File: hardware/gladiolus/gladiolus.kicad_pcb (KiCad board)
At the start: 4 copper layers, 70.7 x 53.3 mm, 7 parts, among them J1 NEIGHBOR1, J2 NEIGHBOR2, J7 BONUS_ROW

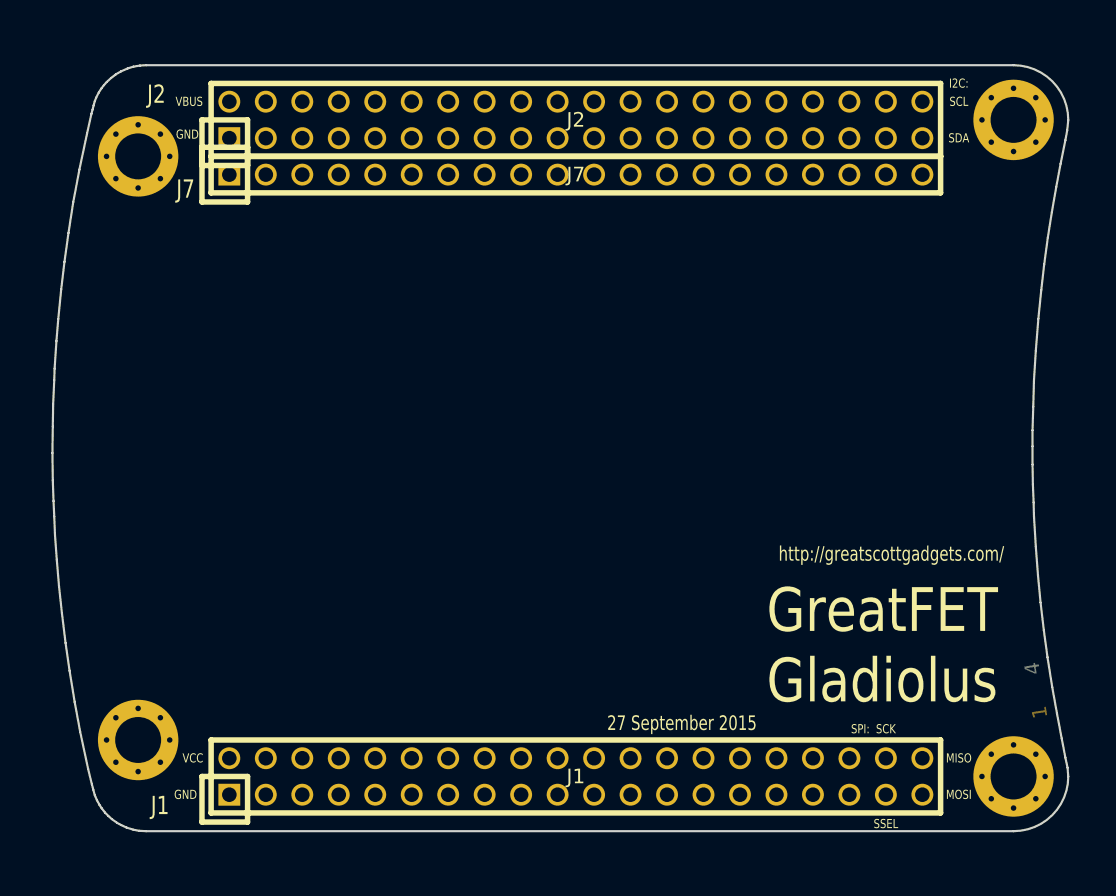
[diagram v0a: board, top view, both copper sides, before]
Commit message: Gladiolus: initial parts placement
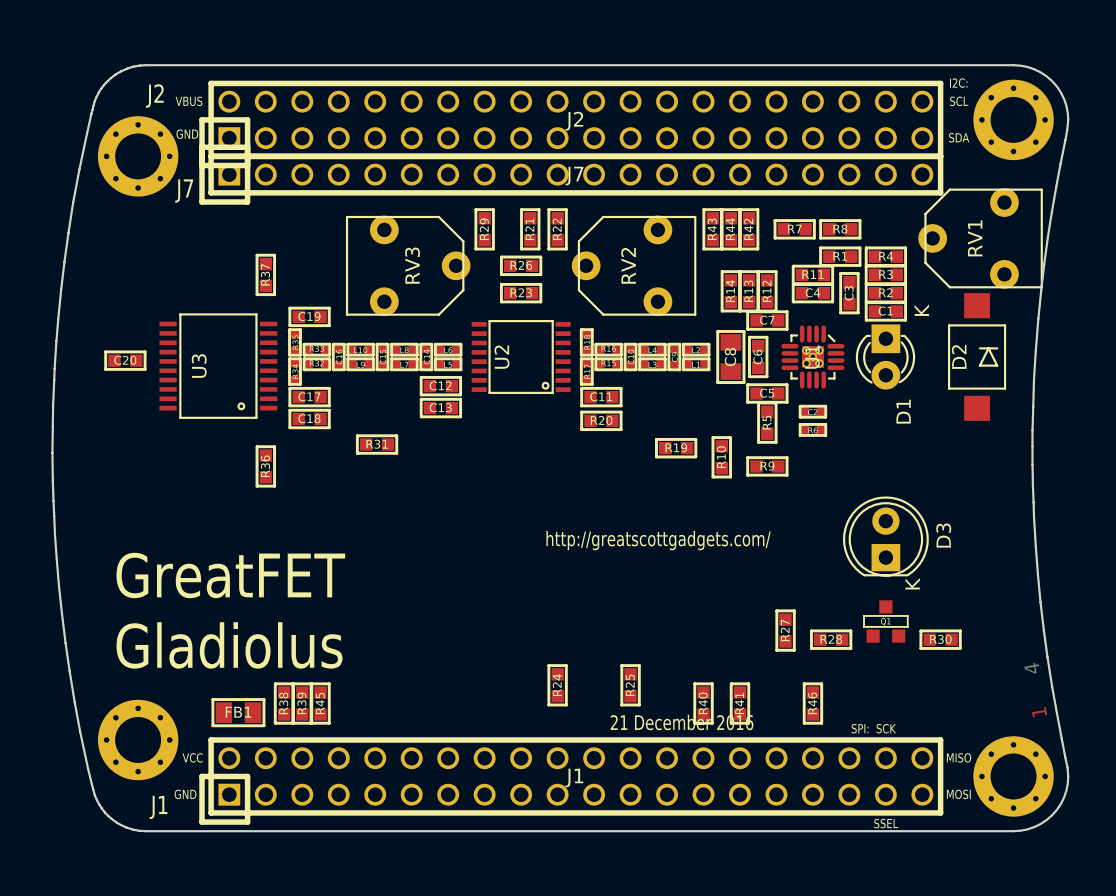
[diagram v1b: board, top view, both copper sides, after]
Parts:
- added C1: C, gsg-modules:0603, F.Cu at (167.6, 85.7)
- added C10: 15pF, gsg-modules:0402, F.Cu at (149.9, 88.9)
- added C11: 100nF, gsg-modules:0603, F.Cu at (147.8, 91.7)
- added C12: 100nF, gsg-modules:0603, F.Cu at (136.7, 90.9)
- added C13: 100nF, gsg-modules:0603, F.Cu at (136.7, 92.5)
- added C14: 130pF, gsg-modules:0402, F.Cu at (135.6, 88.9)
- added C15: 82pF, gsg-modules:0402, F.Cu at (132.6, 88.9)
- added C16: 24pF, gsg-modules:0402, F.Cu at (129.5, 88.9)
- added C17: 100nF, gsg-modules:0603, F.Cu at (127.5, 91.7)
- added C18: 100nF, gsg-modules:0603, F.Cu at (127.5, 93.2)
- added C19: 100nF, gsg-modules:0603, F.Cu at (127.5, 86.1)
- added C2: 15pF, gsg-modules:0402, F.Cu at (162.6, 92.7)
- added C20: 100nF, gsg-modules:0603, F.Cu at (114.7, 89.2)
- added C3: 100nF, gsg-modules:0603, F.Cu at (165.1, 84.5)
- added C4: C, gsg-modules:0603, F.Cu at (162.6, 84.5)
- added C5: 100nF, gsg-modules:0603, F.Cu at (159.4, 91.4)
- added C6: 100nF, gsg-modules:0603, F.Cu at (158.8, 88.9)
- added C7: 100nF, gsg-modules:0603, F.Cu at (159.4, 86.4)
- added C8: 10uF, gsg-modules:0805, F.Cu at (156.8, 88.9)
- added C9: 100pF, gsg-modules:0402, F.Cu at (152.9, 88.9)
- added D1: PHOTODIODE, LEDs:LED-3MM, F.Cu at (167.6, 87.6)
- added D2: PHOTODIODE, gsg-modules:VBPW34FASR, F.Cu at (174.0, 88.9)
- added D3: LED, LEDs:LED-5MM, F.Cu at (167.6, 102.9)
- added FB1: FILTER, gsg-modules:0805, F.Cu at (122.6, 113.7)
- added L1: 2.2uH, gsg-modules:0402, F.Cu at (154.4, 89.4)
- added L10: 1uH, gsg-modules:0402, F.Cu at (131.1, 88.4)
- added L2: 2.2uH, gsg-modules:0402, F.Cu at (154.4, 88.4)
- added L3: 1.5uH, gsg-modules:0402, F.Cu at (151.4, 89.4)
- added L4: 1.5uH, gsg-modules:0402, F.Cu at (151.4, 88.4)
- added L5: 2.2uH, gsg-modules:0402, F.Cu at (137.2, 89.4)
- added L6: 2.2uH, gsg-modules:0402, F.Cu at (137.2, 88.4)
- added L7: 2.2uH, gsg-modules:0402, F.Cu at (134.1, 89.4)
- added L8: 2.2uH, gsg-modules:0402, F.Cu at (134.1, 88.4)
- added L9: 1uH, gsg-modules:0402, F.Cu at (131.1, 89.4)
- added Q1: Q_NPN_BEC, gsg-modules:SOT23-3, F.Cu at (167.6, 107.3)
- added R1: 0, gsg-modules:0603, F.Cu at (164.5, 81.9)
- added R10: 10k, gsg-modules:0603, F.Cu at (156.2, 95.9)
- added R11: R, gsg-modules:0603, F.Cu at (162.6, 83.2)
- added R12: R, gsg-modules:0603, F.Cu at (159.4, 84.3)
- added R13: R, gsg-modules:0603, F.Cu at (158.1, 84.3)
- added R14: R, gsg-modules:0603, F.Cu at (156.8, 84.3)
- added R15: 0, gsg-modules:0402, F.Cu at (148.3, 89.4)
- added R16: 0, gsg-modules:0402, F.Cu at (148.3, 88.4)
- added R17: R, gsg-modules:0402, F.Cu at (146.8, 89.9)
- added R18: R, gsg-modules:0402, F.Cu at (146.8, 87.9)
- added R19: 0, gsg-modules:0603, F.Cu at (153.0, 95.2)
- added R2: 0, gsg-modules:0603, F.Cu at (167.6, 84.5)
- added R20: 0, gsg-modules:0603, F.Cu at (147.8, 93.3)
- added R21: 0, gsg-modules:0603, F.Cu at (142.9, 80.0)
- added R22: 0, gsg-modules:0603, F.Cu at (144.8, 80.0)
- added R23: 0, gsg-modules:0603, F.Cu at (142.2, 84.5)
- added R24: 0, gsg-modules:0603, F.Cu at (144.8, 111.8)
- added R25: 0, gsg-modules:0603, F.Cu at (149.9, 111.8)
- added R26: 0, gsg-modules:0603, F.Cu at (142.2, 82.5)
- added R27: 10k, gsg-modules:0603, F.Cu at (160.7, 108.0)
- added R28: 1k, gsg-modules:0603, F.Cu at (163.8, 108.6)
- added R29: 0, gsg-modules:0603, F.Cu at (139.7, 80.0)
- added R3: 0, gsg-modules:0603, F.Cu at (167.6, 83.2)
- added R30: 75, gsg-modules:0603, F.Cu at (171.4, 108.6)
- added R31: 0, gsg-modules:0603, F.Cu at (132.2, 95.0)
- added R32: 0, gsg-modules:0402, F.Cu at (128.0, 89.4)
- added R33: 0, gsg-modules:0402, F.Cu at (128.0, 88.4)
- added R34: R, gsg-modules:0402, F.Cu at (126.5, 89.9)
- added R35: R, gsg-modules:0402, F.Cu at (126.5, 87.9)
- added R36: 10k, gsg-modules:0603, F.Cu at (124.5, 96.5)
- added R37: R, gsg-modules:0603, F.Cu at (124.5, 83.2)
- added R38: 39, gsg-modules:0603, F.Cu at (125.7, 113.0)
- added R39: 39, gsg-modules:0603, F.Cu at (127.0, 113.0)
- added R4: 0, gsg-modules:0603, F.Cu at (167.6, 81.9)
- added R40: 39, gsg-modules:0603, F.Cu at (154.9, 113.0)
- added R41: 39, gsg-modules:0603, F.Cu at (157.5, 113.0)
- added R42: 39, gsg-modules:0603, F.Cu at (158.1, 80.0)
- added R43: 39, gsg-modules:0603, F.Cu at (155.6, 80.0)
- added R44: 39, gsg-modules:0603, F.Cu at (156.8, 80.0)
- added R45: 39, gsg-modules:0603, F.Cu at (128.3, 113.0)
- added R46: 39, gsg-modules:0603, F.Cu at (162.6, 113.0)
- added R5: R, gsg-modules:0603, F.Cu at (159.4, 93.5)
- added R6: 100k, gsg-modules:0402, F.Cu at (162.6, 94.0)
- added R7: 3.24k, gsg-modules:0603, F.Cu at (161.3, 80.0)
- added R8: 1.74k, gsg-modules:0603, F.Cu at (164.5, 80.0)
- added R9: 0, gsg-modules:0603, F.Cu at (159.4, 96.5)
- added RV1: POT, gsg-modules:3306F, F.Cu at (175.9, 80.6)
- added RV2: POT, gsg-modules:3306F, F.Cu at (151.8, 82.5)
- added RV3: POT, gsg-modules:3306F, F.Cu at (132.7, 82.5)
- added U1: THS4520RGT, gsg-modules:QFN16-3, F.Cu at (162.6, 88.9)
- added U2: AD8330ARQZ, gsg-modules:TSSOP16, F.Cu at (142.2, 88.9)
- added U3: AD9283, gsg-modules:SSOP20, F.Cu at (121.2, 89.5)
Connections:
- J1 pad 10: (no net) -> /P1_1
- J1 pad 11: (no net) -> /CLK0
- J1 pad 12: (no net) -> /P1_2
- J1 pad 13: (no net) -> /P1_5
- J1 pad 14: (no net) -> /P5_2
- J1 pad 15: (no net) -> /P1_7
- J1 pad 16: (no net) -> /P1_6
- J1 pad 17: (no net) -> /P1_9
- J1 pad 18: (no net) -> /P1_8
- J1 pad 19: (no net) -> /P5_3
- J1 pad 2: VCC -> Net-(FB1-Pad2)
- J1 pad 20: (no net) -> /P1_10
- J1 pad 21: (no net) -> /P1_12
- J1 pad 22: (no net) -> /P1_11
- J1 pad 23: (no net) -> /P5_5
- J1 pad 24: (no net) -> /P5_4
- J1 pad 25: (no net) -> /P1_14
- J1 pad 26: (no net) -> /P1_13
- J1 pad 27: (no net) -> /P5_6
- J1 pad 28: (no net) -> /P1_15
- J1 pad 29: (no net) -> /P5_7
- J1 pad 3: (no net) -> /P4_9
- J1 pad 30: (no net) -> /P1_16
- J1 pad 31: (no net) -> /P1_18
- J1 pad 32: (no net) -> /P1_17
- J1 pad 33: (no net) -> /P9_5
- J1 pad 34: (no net) -> /P9_6
- J1 pad 35: (no net) -> /P2_0
- J1 pad 36: (no net) -> /P6_0
- J1 pad 37: (no net) -> /P1_20
- J1 pad 38: (no net) -> /P1_19
- J1 pad 39: (no net) -> /P1_4
- J1 pad 4: (no net) -> /P0_0
- J1 pad 40: (no net) -> /P1_3
- J1 pad 5: (no net) -> /P4_10
- J1 pad 6: (no net) -> /P0_1
- J1 pad 7: (no net) -> /P1_0
- J1 pad 8: (no net) -> /P5_0
- J1 pad 9: (no net) -> /P5_1
- J2 pad 10: (no net) -> /P4_6
- J2 pad 11: (no net) -> /P4_7
- J2 pad 12: (no net) -> /CLK2
- J2 pad 13: (no net) -> /P2_8
- J2 pad 14: (no net) -> /P2_7
- J2 pad 15: (no net) -> /P2_6
- J2 pad 16: (no net) -> /P7_7
- J2 pad 17: (no net) -> /WAKEUP0
- J2 pad 18: (no net) -> /P2_5
- J2 pad 19: (no net) -> /P2_4
- J2 pad 20: (no net) -> /P2_3
- J2 pad 21: (no net) -> /PF_4
- J2 pad 22: (no net) -> /P3_2
- J2 pad 23: (no net) -> /P7_2
- J2 pad 24: (no net) -> /P3_1
- J2 pad 25: (no net) -> /P7_1
- J2 pad 26: (no net) -> /P3_0
- J2 pad 27: (no net) -> /P7_0
- J2 pad 28: (no net) -> /P3_4
- J2 pad 29: (no net) -> /P6_8
- J2 pad 3: (no net) -> /P4_8
- J2 pad 30: (no net) -> /P3_7
- J2 pad 31: (no net) -> /P6_7
- J2 pad 32: (no net) -> /P3_3
- J2 pad 33: (no net) -> /P2_2
- J2 pad 34: (no net) -> /P6_6
- J2 pad 35: (no net) -> /P2_1
- J2 pad 36: (no net) -> /P6_3
- J2 pad 37: (no net) -> /P3_5
- J2 pad 38: (no net) -> /P3_6
- J2 pad 39: (no net) -> /I2C0_SDA
- J2 pad 4: (no net) -> /P4_0
- J2 pad 40: (no net) -> /I2C0_SCL
- J2 pad 5: (no net) -> /ADC0_0
- J2 pad 6: (no net) -> /P4_5
- J2 pad 7: (no net) -> /P4_4
- J2 pad 8: (no net) -> /P4_2
- J2 pad 9: (no net) -> /P4_3
- J7 pad 11: (no net) -> /RESET
- J7 pad 12: (no net) -> /VBAT
- J7 pad 13: (no net) -> /P2_11
- J7 pad 14: (no net) -> /P2_10
- J7 pad 15: (no net) -> /P6_10
- J7 pad 16: (no net) -> /P6_9
- J7 pad 17: (no net) -> /P6_2
- J7 pad 18: (no net) -> /P6_1
- J7 pad 2: (no net) -> /P6_4
- J7 pad 20: VCC -> Net-(J7-Pad20)
- J7 pad 3: (no net) -> /P6_5
- J7 pad 4: (no net) -> /ADC0_5
- J7 pad 5: (no net) -> /ADC0_2
- J7 pad 6: (no net) -> /P2_9
- J7 pad 7: (no net) -> /P2_12
- J7 pad 8: (no net) -> /P2_13
- J7 pad 9: (no net) -> /RTC_ALARM
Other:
- board text added: "21 December 2016"
- board text removed: "27 September 2015"

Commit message: Gladiolus: reversed potentiometers
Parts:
- turned R43 to 270 degrees
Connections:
- RV1 pad 1: VCC -> GND
- RV1 pad 3: GND -> VCC
- RV2 pad 1: VCC -> GND
- RV2 pad 3: GND -> VCC
- RV3 pad 1: VCC -> GND
- RV3 pad 3: GND -> VCC
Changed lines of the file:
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@@
     (links 228)
     (no_connects 172)
-    (area 63.017399 66.04 279.525801 196.007778)
+    (area 109.525999 68.504999 180.415001 121.995001)
     (thickness 1.6)
     (drawings 122)
@@
   )
   (module gsg-modules:0603 (layer F.Cu)
-    (at 155.575 80.01 90)
-    (solder_mask_margin 0.1016)
-    (fp_text reference R43 (at 0 0 90) (layer F.SilkS)
-      (effects (font (size 0.6096 0.6096) (thickness 0.1524)))
-    )
-    (fp_text value 39 (at 0 0 90) (layer F.SilkS) hide
-      (effects (font (size 0.6096 0.6096) (thickness 0.1524)))
-    )
-    (fp_line (start 1.3716 -0.6096) (end -1.3716 -0.6096) (layer F.SilkS) (width 0.2032))
-    (fp_line (start -1.3716 -0.6096) (end -1.3716 0.6096) (layer F.SilkS) (width 0.2032))
-    (fp_line (start -1.3716 0.6096) (end 1.3716 0.6096) (layer F.SilkS) (width 0.2032))
-    (fp_line (start 1.3716 0.6096) (end 1.3716 -0.6096) (layer F.SilkS) (width 0.2032))
-    (pad 2 smd rect (at 0.762 0 90) (size 0.8636 0.8636) (layers F.Cu F.Paste F.Mask)
+    (at 155.575 80.01 270)
+    (solder_mask_margin 0.1016)
+    (fp_text reference R43 (at 0 0 270) (layer F.SilkS)
+      (effects (font (size 0.6096 0.6096) (thickness 0.1524)))
+    )
+    (fp_text value 39 (at 0 0 270) (layer F.SilkS) hide
+      (effects (font (size 0.6096 0.6096) (thickness 0.1524)))
+    )
+    (fp_line (start 1.3716 -0.6096) (end -1.3716 -0.6096) (layer F.SilkS) (width 0.2032))
+    (fp_line (start -1.3716 -0.6096) (end -1.3716 0.6096) (layer F.SilkS) (width 0.2032))
+    (fp_line (start -1.3716 0.6096) (end 1.3716 0.6096) (layer F.SilkS) (width 0.2032))
+    (fp_line (start 1.3716 0.6096) (end 1.3716 -0.6096) (layer F.SilkS) (width 0.2032))
+    (pad 2 smd rect (at 0.762 0 270) (size 0.8636 0.8636) (layers F.Cu F.Paste F.Mask)
       (net 139 /D5) (solder_mask_margin 0.1016) (clearance 0.1778))
-    (pad 1 smd rect (at -0.762 0 90) (size 0.8636 0.8636) (layers F.Cu F.Paste F.Mask)
+    (pad 1 smd rect (at -0.762 0 270) (size 0.8636 0.8636) (layers F.Cu F.Paste F.Mask)
       (net 94 /P6_6) (solder_mask_margin 0.1016) (clearance 0.1778))
   )
@@
     (fp_line (start -3.4 2.6) (end -3.4 -3.8) (layer F.SilkS) (width 0.15))
     (pad 1 thru_hole circle (at -2.5 0 90) (size 2 2) (drill 1) (layers *.Cu *.Mask)
-      (net 2 VCC))
+      (net 1 GND))
     (pad 2 thru_hole circle (at 0 -5 90) (size 2 2) (drill 1) (layers *.Cu *.Mask)
       (net 7 "Net-(C3-Pad1)"))
     (pad 3 thru_hole circle (at 2.5 0 90) (size 2 2) (drill 1) (layers *.Cu *.Mask)
-      (net 1 GND))
+      (net 2 VCC))
   )
   (module gsg-modules:3306F (layer F.Cu)
@@
     (fp_line (start -3.4 2.6) (end -3.4 -3.8) (layer F.SilkS) (width 0.15))
     (pad 1 thru_hole circle (at -2.5 0 90) (size 2 2) (drill 1) (layers *.Cu *.Mask)
-      (net 2 VCC))
+      (net 1 GND))
     (pad 2 thru_hole circle (at 0 -5 90) (size 2 2) (drill 1) (layers *.Cu *.Mask)
       (net 127 "Net-(R21-Pad1)"))
     (pad 3 thru_hole circle (at 2.5 0 90) (size 2 2) (drill 1) (layers *.Cu *.Mask)
-      (net 1 GND))
+      (net 2 VCC))
   )
   (module gsg-modules:3306F (layer F.Cu)
@@
     (fp_line (start -3.4 2.6) (end -3.4 -3.8) (layer F.SilkS) (width 0.15))
     (pad 1 thru_hole circle (at -2.5 0 270) (size 2 2) (drill 1) (layers *.Cu *.Mask)
-      (net 2 VCC))
+      (net 1 GND))
     (pad 2 thru_hole circle (at 0 -5 270) (size 2 2) (drill 1) (layers *.Cu *.Mask)
       (net 130 "Net-(R29-Pad1)"))
     (pad 3 thru_hole circle (at 2.5 0 270) (size 2 2) (drill 1) (layers *.Cu *.Mask)
-      (net 1 GND))
+      (net 2 VCC))
   )
   (module gsg-modules:QFN16-3 (layer F.Cu)

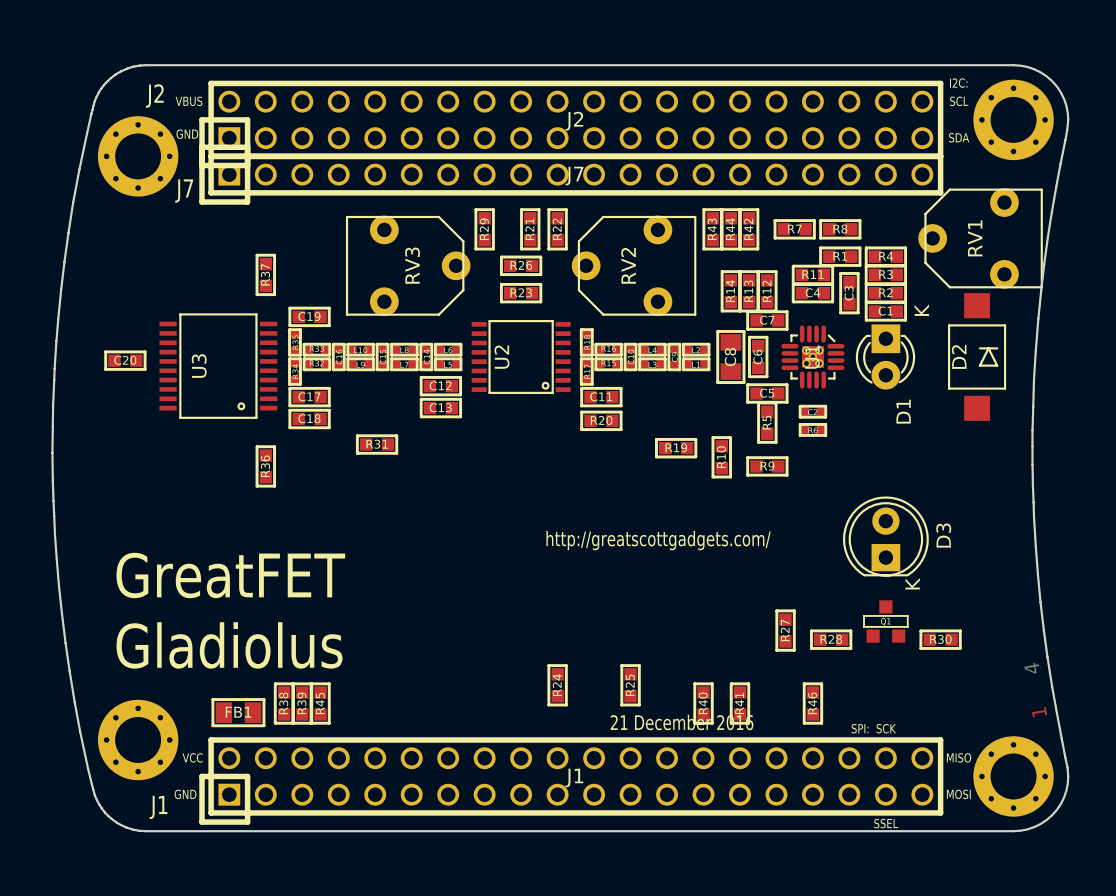
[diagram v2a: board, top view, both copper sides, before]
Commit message: Gladiolus: completed initial layout
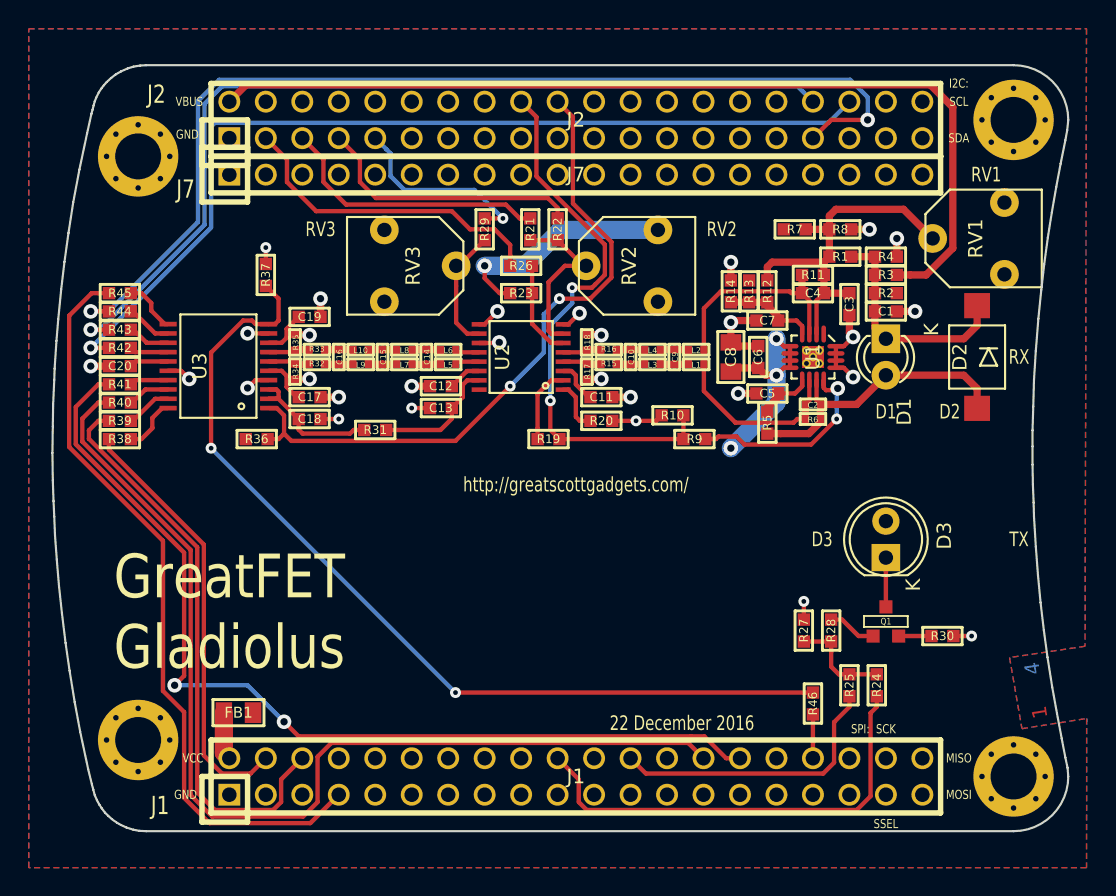
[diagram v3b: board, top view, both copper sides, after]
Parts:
- moved R41 48.6 mm to (114.3, 90.8), turned to 0 degrees
- moved R40 45.7 mm to (114.3, 92.1), turned to 0 degrees
- moved R42 44.6 mm to (114.3, 88.3), turned to 0 degrees
- moved R44 42.9 mm to (114.3, 85.7), turned to 0 degrees
- moved R43 41.9 mm to (114.3, 87.0), turned to 0 degrees
- moved R45 31.8 mm to (114.3, 84.5), turned to 0 degrees
- moved R39 23.4 mm to (114.3, 93.3), turned to 0 degrees
- moved R24 22.2 mm to (167.0, 111.8)
- moved R38 21.7 mm to (114.3, 94.6), turned to 0 degrees
- moved R25 15.2 mm to (165.1, 111.8)
- moved R19 8.91 mm to (144.1, 94.6)
- moved R9 5.43 mm to (154.3, 94.6)
- moved R10 4.50 mm to (152.8, 93.0), turned to 0 degrees
- moved R36 2.01 mm to (123.8, 94.6), turned to 180 degrees
- moved R27 1.27 mm to (161.9, 108.0)
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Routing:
- net /P2_2: track 0.00 -> 73.4 mm, vias 0 -> 2
- net /P1_15: track 0.00 -> 72.4 mm
- net /P1_16: track 0.00 -> 67.2 mm, vias 0 -> 2
- net /VBUS: track 0.00 -> 66.0 mm
- net /P6_3: track 0.00 -> 65.3 mm, vias 0 -> 1
- net /ADCCLK: track 0.00 -> 64.2 mm, vias 0 -> 2
- net /P6_6: track 0.00 -> 64.0 mm, vias 0 -> 1
- net /P1_0: track 0.00 -> 52.6 mm
- net GND: track 0.00 -> 47.3 mm, vias 0 -> 29
- net VCC: track 0.00 -> 47.0 mm, vias 0 -> 4
- net /P2_3: track 0.00 -> 46.9 mm, vias 0 -> 2
- net /P0_1: track 0.00 -> 40.3 mm
- net /P2_5: track 0.00 -> 38.8 mm, vias 0 -> 2
- net /P1_10: track 0.00 -> 31.8 mm
- net /P0_0: track 0.00 -> 30.0 mm
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- added copper zone on B.Cu, net GND
- added copper zone on F.Cu, net VCC
- removed copper zone on C2.Cu, net GND
- removed copper zone on C3.Cu, net VCC
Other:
- board text added: "22 December 2016"
- board text added: "D1"
- board text added: "D2"
- board text added: "D3"
- board text added: "RV1"
- board text added: "RV2"
- board text added: "RV3"
- board text added: "RX"
- board text added: "TX"
- board text removed: "21 December 2016"
